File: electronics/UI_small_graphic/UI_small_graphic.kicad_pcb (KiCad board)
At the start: 2 copper layers, 50 x 50 mm, 45 parts, among them J1 Conn_01x06, U1 128x32, U2 128x64, U3 PCF8574, U4 PCA9554

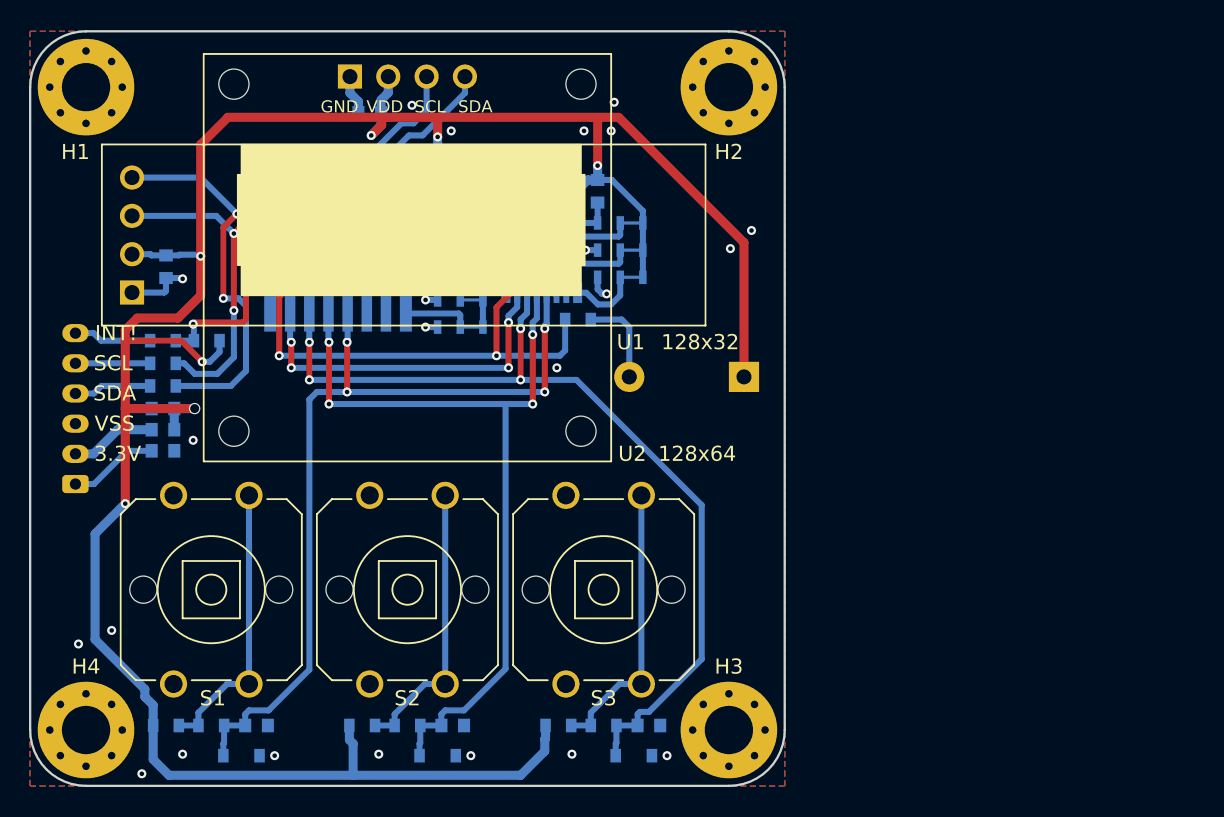
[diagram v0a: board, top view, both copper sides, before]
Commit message: added new displays and addional buttons
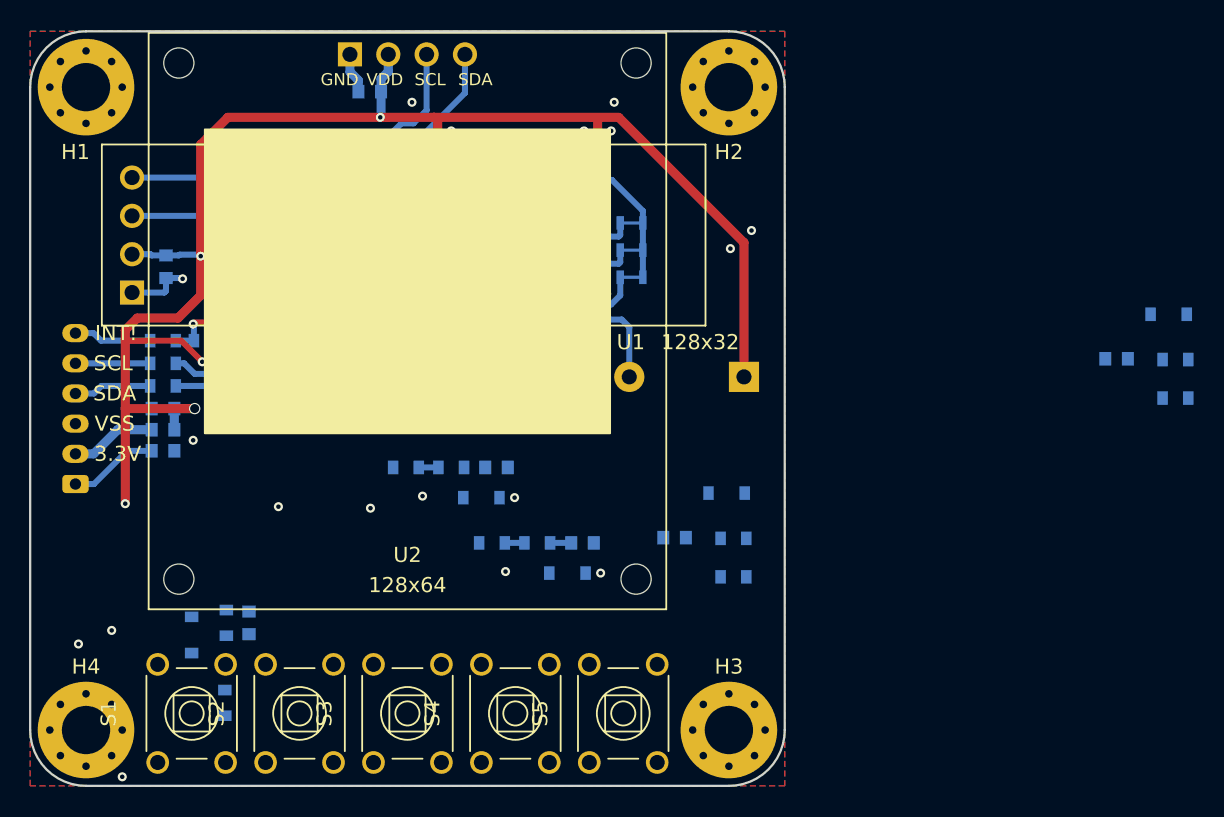
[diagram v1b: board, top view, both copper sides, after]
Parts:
- added C10: 100n, SquantorRcl:C_0603, B.Cu at (222.0, 71.7)
- added C9: 100n, SquantorRcl:C_0603, B.Cu at (192.7, 83.5)
- added D4: SD05, SquantorDiodes:SOD_323_onsemi, B.Cu at (196.2, 80.6)
- added D5: SD05, SquantorDiodes:SOD_323_onsemi, B.Cu at (225.4, 68.8)
- added R12: 100, SquantorRcl:R_0603_hand, B.Cu at (196.6, 83.6)
- added R13: 4.7K, SquantorRcl:R_0603_hand, B.Cu at (196.6, 86.2)
- added R14: 100, SquantorRcl:R_0603_hand, B.Cu at (225.9, 74.3)
- added R15: 4.7K, SquantorRcl:R_0603_hand, B.Cu at (225.9, 71.8)
- added S4: BUT3, SquantorSwitches:Omron_B3F-1052, F.Cu at (182.2, 95.2)
- added S5: BUT4, SquantorSwitches:Omron_B3F-1052, F.Cu at (189.3, 95.2)
- S1, S2, S3: footprint SquantorSwitches:Omron_B3F-4055 -> SquantorSwitches:Omron_B3F-1052
- U2: footprint SquantorModules:OLED_128x64 -> SquantorModules:OLED_132in_128x96
- moved C5 17.3 mm to (180.9, 78.9)
- moved D2 17.3 mm to (179.9, 80.9)
- moved R7 17.3 mm to (177.9, 78.9)
- moved R9 17.3 mm to (174.9, 78.9)
- moved S3 15.4 mm to (175.0, 95.2)
- moved C6 12.9 mm to (186.6, 83.9)
- moved D3 12.9 mm to (185.6, 85.9)
- moved R10 12.9 mm to (180.6, 83.9)
- moved R8 12.9 mm to (183.6, 83.9)
- moved S2 10.9 mm to (167.8, 95.2)
- moved D1 8.65 mm to (160.7, 90.0), turned to -90 degrees
- moved S1 8.30 mm to (160.7, 95.2)
- moved R5 6.87 mm to (163.0, 89.2), turned to 90 degrees
- moved C4 6.82 mm to (164.5, 89.2), turned to -90 degrees
- moved U2 4.20 mm to (175.0, 69.2)
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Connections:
- U3 pad 9: unconnected-(U3-Pad9) -> /BUTT4
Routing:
- net /3.3V: track 188.4 -> 135.5 mm
- net /BUTT2: track 59.9 -> 29.5 mm
- net /BUTT0: track 55.2 -> 27.6 mm
- net /BUTT1: track 54.0 -> 27.1 mm
- net Net-(R5-Pad1): track 18.8 -> 0.00 mm
- net Net-(R10-Pad2): track 18.8 -> 1.30 mm
- net Net-(R7-Pad1): track 18.7 -> 1.30 mm
- net /SDA: track 63.1 -> 64.6 mm
- net /SCL: track 57.1 -> 58.6 mm

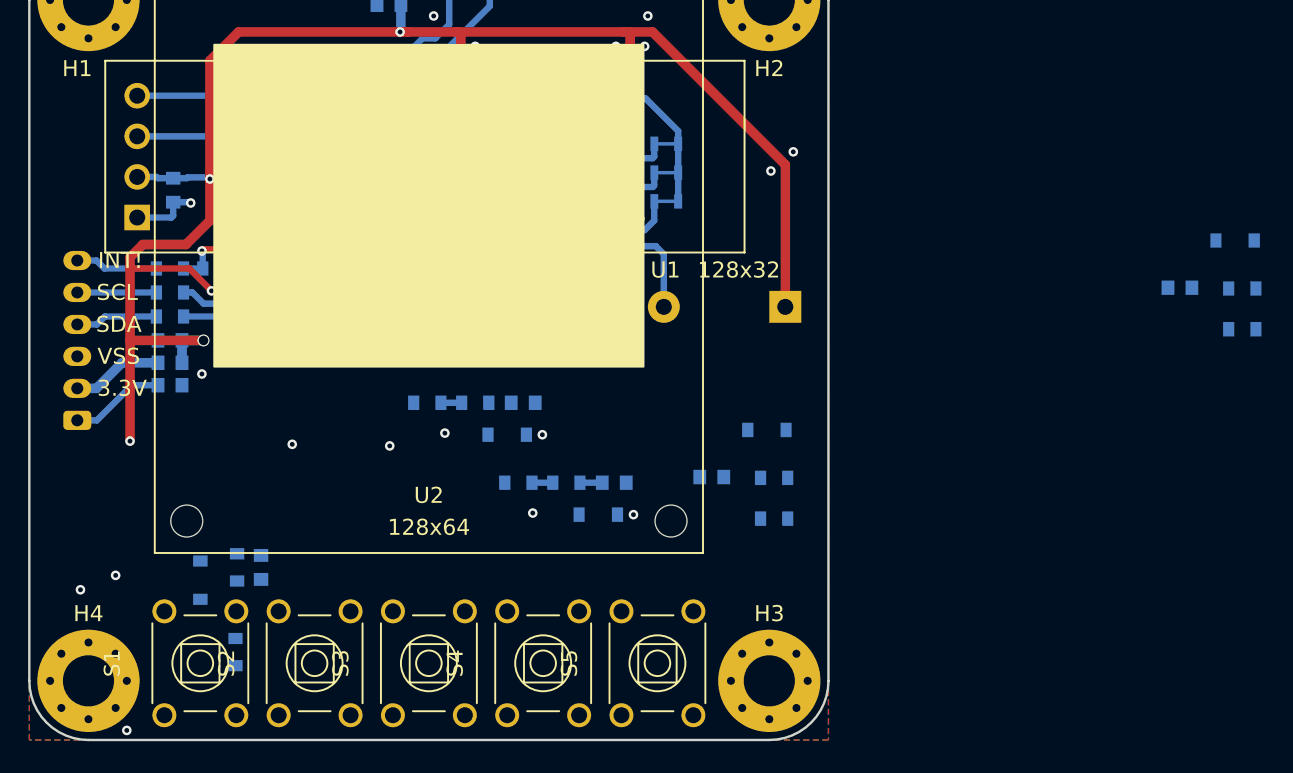
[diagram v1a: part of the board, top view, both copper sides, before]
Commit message: placed ESD parts, silk placed
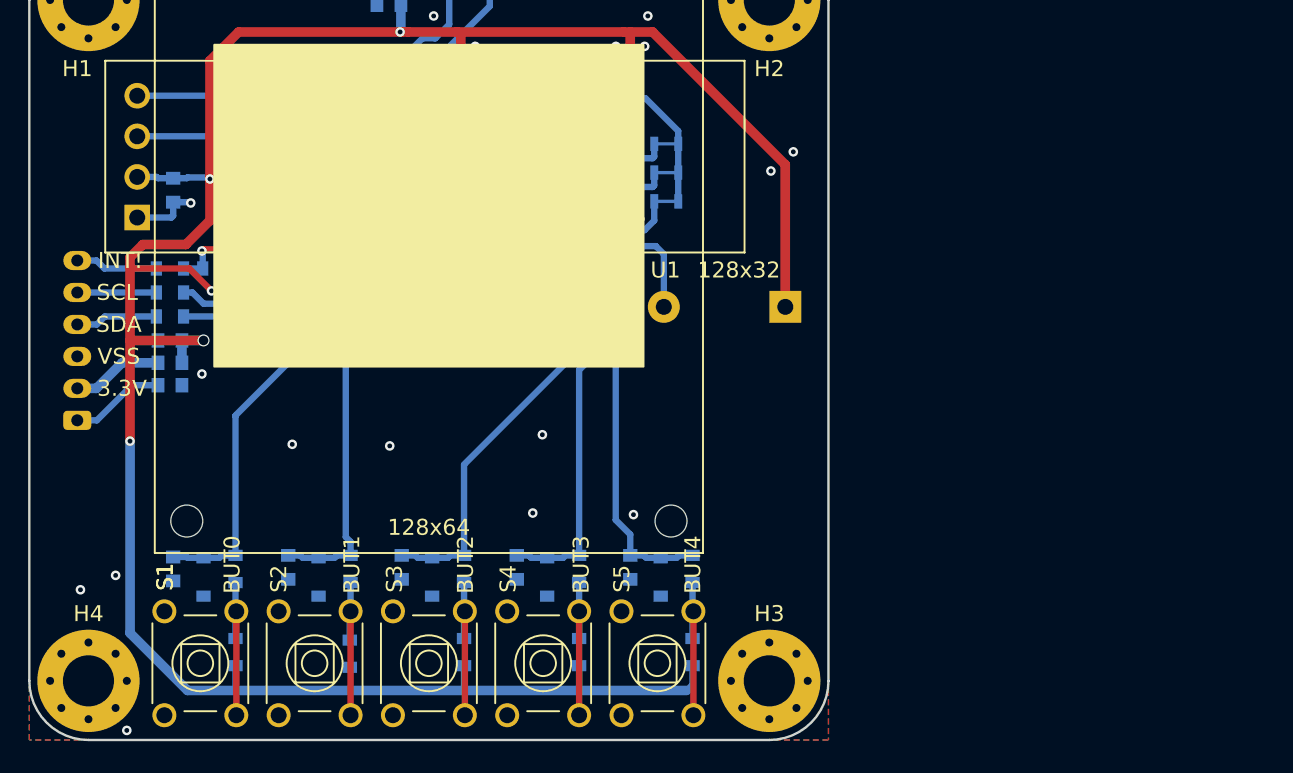
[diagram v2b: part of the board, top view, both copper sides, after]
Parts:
- moved D5 41.7 mm to (189.5, 89.8), turned to -90 degrees
- moved R15 41.2 mm to (191.5, 94.5), turned to 90 degrees
- moved C10 38.6 mm to (187.6, 89.2), turned to -90 degrees
- moved R14 37.5 mm to (191.5, 89.3), turned to 90 degrees
- moved C5 17.9 mm to (166.2, 89.2), turned to -90 degrees
- moved D4 16.5 mm to (182.4, 89.8), turned to -90 degrees
- moved R9 16.4 mm to (170.1, 94.6), turned to 90 degrees
- moved R13 14.8 mm to (184.4, 94.5), turned to 90 degrees
- moved D2 14.8 mm to (168.1, 89.8), turned to -90 degrees
- moved C6 14.3 mm to (173.3, 89.2), turned to -90 degrees
- moved R12 13.5 mm to (184.4, 89.3), turned to 90 degrees
- moved C9 13.4 mm to (180.5, 89.2), turned to -90 degrees
- moved R7 13.0 mm to (170.1, 89.3), turned to 90 degrees
- moved R10 11.1 mm to (177.2, 94.5), turned to 90 degrees
- moved D3 11.1 mm to (175.2, 89.8), turned to -90 degrees
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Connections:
- C10 pad 2: Net-(C10-Pad2) -> /VSS
- C9 pad 2: Net-(C9-Pad2) -> /VSS
- D4 pad 2: Net-(C9-Pad2) -> /VSS
- D5 pad 2: Net-(C10-Pad2) -> /VSS
- U4 pad 9: unconnected-(U4-Pad9) -> /BUTT4
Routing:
- net /BUTT4: track 0.00 -> 65.5 mm, vias 0 -> 4
- net /3.3V: track 135.5 -> 190.2 mm
- net /BUTT3: track 23.2 -> 48.2 mm
- net /BUTT0: track 27.6 -> 49.0 mm
- net /BUTT2: track 29.5 -> 49.8 mm
- net /BUTT1: track 27.1 -> 45.4 mm
- net Net-(R14-Pad1): track 0.00 -> 10.0 mm
- net Net-(R5-Pad1): track 0.00 -> 10.0 mm
- net Net-(R12-Pad1): track 0.00 -> 10.0 mm
- net Net-(R7-Pad1): track 1.30 -> 10.1 mm
- net Net-(R10-Pad2): track 1.30 -> 10.0 mm
- net /BUZZ: track 45.4 -> 44.9 mm
- net /VSS: vias 27 -> 26

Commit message: updated versionnumber
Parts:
- N2: value V20220603 -> V20220828
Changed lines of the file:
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@@
       (effects (font (size 1 1) (thickness 0.15)) (justify mirror))
     )
-    (fp_text value "V20220603" (at 0.8 0.1) (layer "B.SilkS")
+    (fp_text value "V20220828" (at 0.8 0.1) (layer "B.SilkS")
       (effects (font (size 0.8 0.8) (thickness 0.15)) (justify mirror))
     )

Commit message: updated versionnumber
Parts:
- N2: value V20220828 -> V20220916
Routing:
- net /3.3V: track 190.2 -> 191.7 mm
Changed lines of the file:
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@@
       (effects (font (size 1 1) (thickness 0.15)) (justify mirror))
     )
-    (fp_text value "V20220828" (at 0.8 0.1) (layer "B.SilkS")
+    (fp_text value "V20220916" (at 0.8 0.1) (layer "B.SilkS")
       (effects (font (size 0.8 0.8) (thickness 0.15)) (justify mirror))
     )
@@
   (segment (start 190.6 64.5) (end 190.6 62.7) (width 0.4) (layer "B.Cu") (net 9))
   (segment (start 190.6 62.7) (end 190.6 61.9) (width 0.4) (layer "B.Cu") (net 9))
+  (segment (start 170.053 95.45) (end 170.053 96.901) (width 0.4) (layer "B.Cu") (net 9))
   (segment (start 191.5 96.536) (end 191.135 96.901) (width 0.4) (layer "B.Cu") (net 9))
   (segment (start 163.068 96.901) (end 170.053 96.901) (width 0.6) (layer "B.Cu") (net 9))

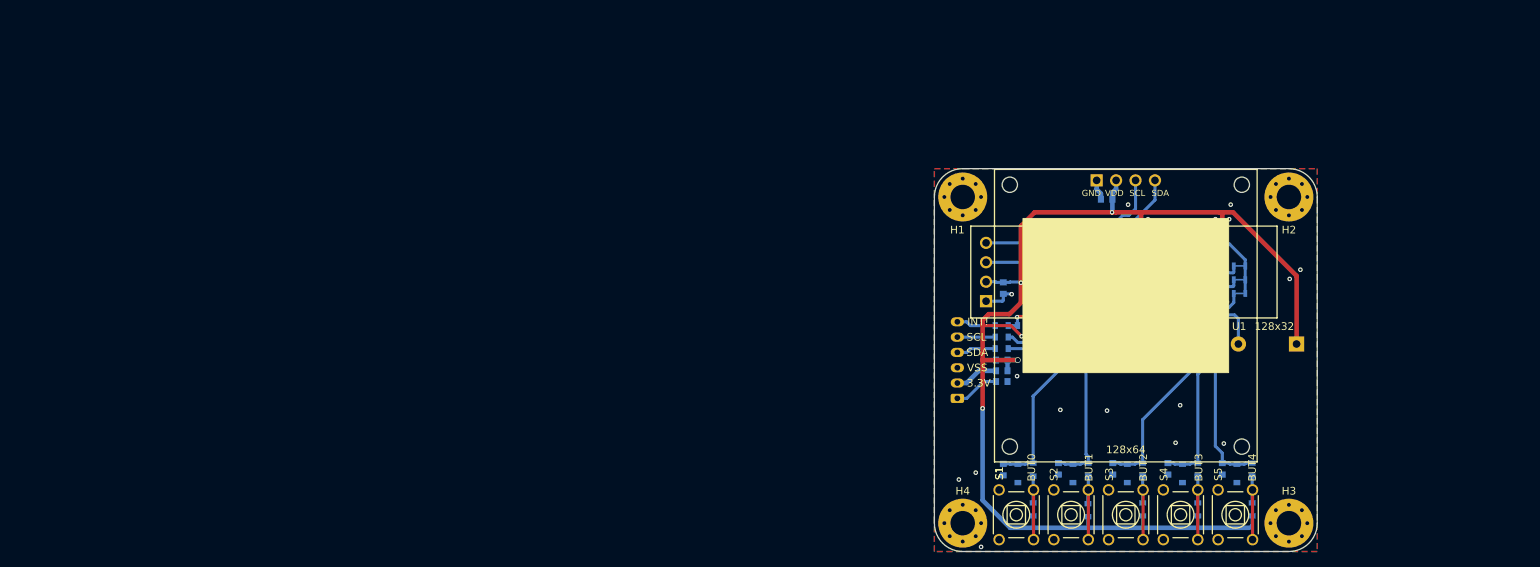
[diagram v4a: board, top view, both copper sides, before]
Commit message: updated to new kicad version, updated mechanical dimensions to newer nuclone hole pattern
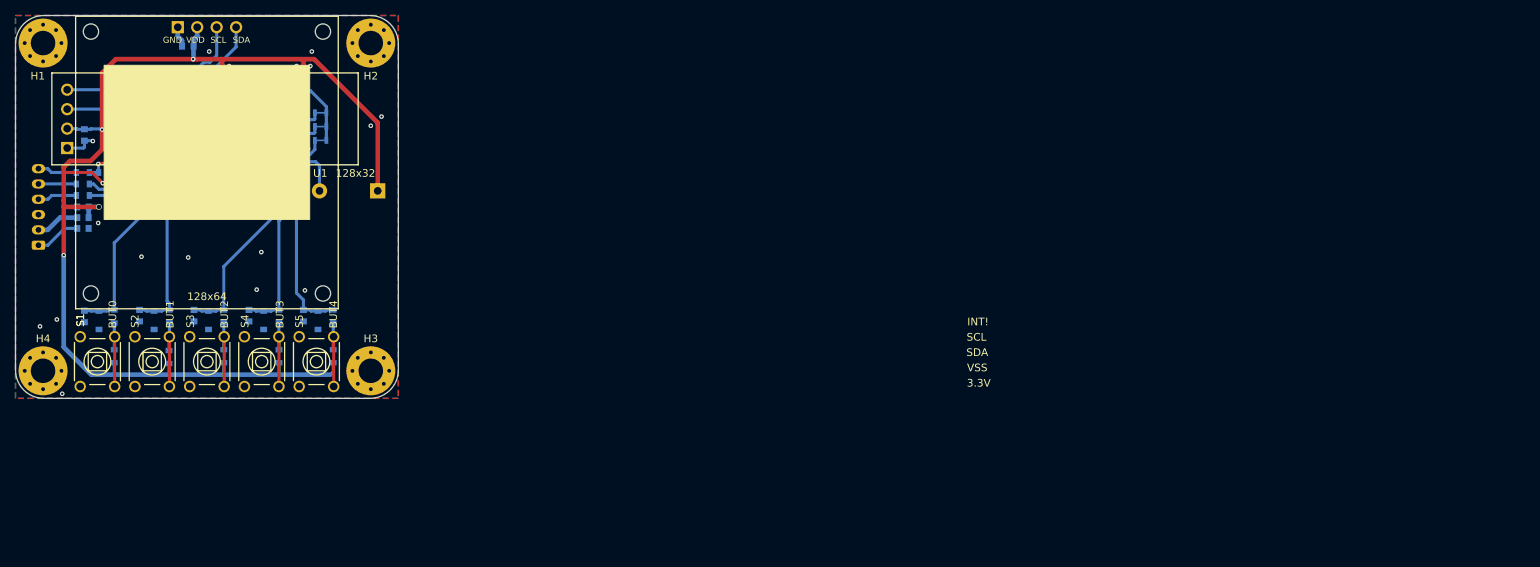
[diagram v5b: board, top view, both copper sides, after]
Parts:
- moved H1 121.8 mm to (33.6, 33.6)
- moved H4 121.7 mm to (33.6, 76.4)
- moved BZ1 121.7 mm to (77.3, 52.9)
- moved FB1 121.7 mm to (38.8, 56.4)
- moved C1 121.7 mm to (38.8, 55.0)
- moved C6 121.7 mm to (53.3, 69.2)
- moved FB2 121.7 mm to (38.8, 57.8)
- moved JP3 121.7 mm to (58.5, 45.9)
- moved R1 121.7 mm to (38.8, 53.5)
- moved R11 121.7 mm to (66.3, 49.1)
- moved R2 121.7 mm to (38.8, 52.0)
- moved R3 121.7 mm to (38.8, 50.5)
- moved S5 121.7 mm to (69.3, 75.2)
- moved U4 121.7 mm to (63.9, 44.4)
- moved C10 121.7 mm to (67.6, 69.2)
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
